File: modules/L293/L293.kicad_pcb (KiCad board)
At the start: 2 copper layers, 40.6 x 40.6 mm, 40 parts, among them J1 2, J10 11, J11 12, J12 13, J13 A0, J14 A1, J15 A2, J16 A3, J17 A4, J18 A5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

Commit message: Small fixes
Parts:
- moved C2 22.9 mm to (108.3, 62.8)
- moved J16 22.9 mm to (92.7, 52.1)
- moved J18 22.9 mm to (92.7, 57.1)
- moved J2 22.9 mm to (125.7, 57.1)
- moved J4 22.9 mm to (125.7, 52.1)
- moved JP1 22.9 mm to (95.9, 57.1)
- moved U2 22.9 mm to (119.0, 45.8)
- moved U3 22.9 mm to (119.0, 42.2)
- moved C1 22.9 mm to (116.1, 48.6)
- moved C5 22.9 mm to (97.8, 64.8)
- moved C6 22.9 mm to (104.8, 62.0)
- moved H1 22.9 mm to (92.7, 31.8)
- moved H2 22.9 mm to (92.7, 64.8)
- moved H3 22.9 mm to (125.7, 31.8)
- moved H4 22.9 mm to (125.7, 64.8)
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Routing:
- net (no net): track 5.72 -> 8.26 mm
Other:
- board text added: "28.03.2020"
- board text removed: "26.03.2020"

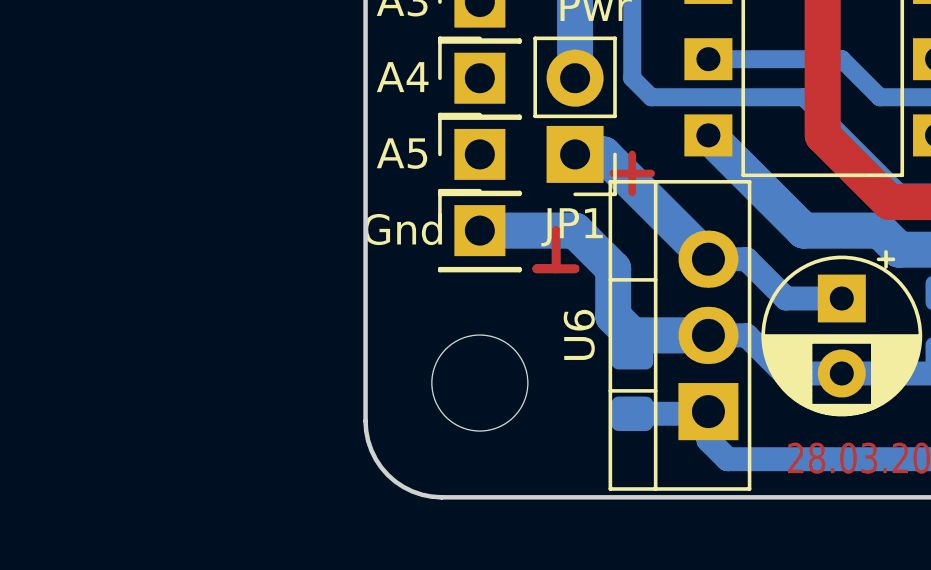
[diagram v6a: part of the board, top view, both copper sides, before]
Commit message: Motor shield v2 in work Attention! Pin numbers changed!
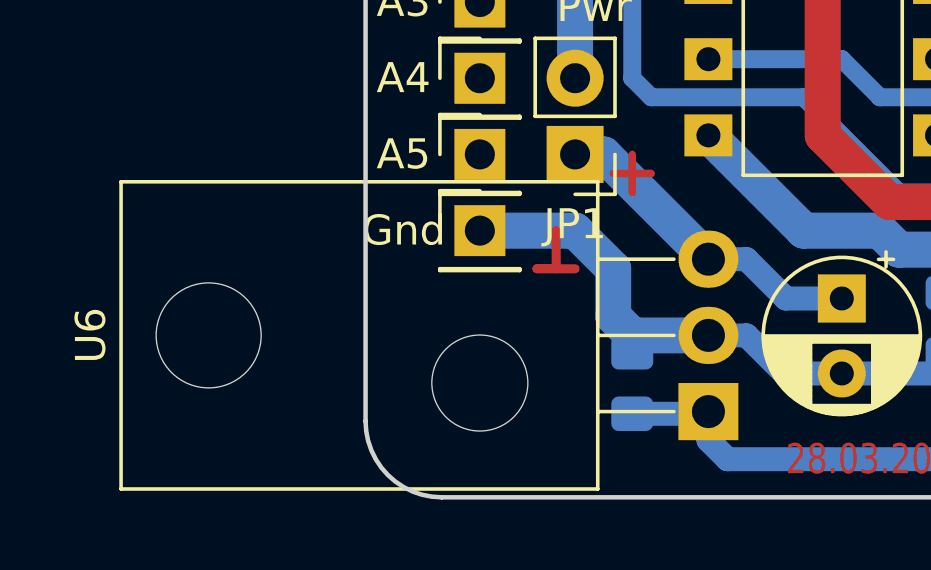
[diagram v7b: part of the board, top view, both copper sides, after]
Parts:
- U6: footprint Package_TO_SOT_THT:TO-220-3_Vertical -> Package_TO_SOT_THT:TO-220-3_Horizontal_TabDown
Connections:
- J10 pad 1: Net-(J10-Pad1) -> /M2-
- J4 pad 1: Net-(J4-Pad1) -> /PWM1
- J5 pad 1: Net-(J5-Pad1) -> /PWM2
- J7 pad 1: Net-(J7-Pad1) -> /M1+
- J8 pad 1: Net-(J8-Pad1) -> /M1-
- J9 pad 1: Net-(J9-Pad1) -> /M2+
- U1 pad 1: Net-(J3-Pad1) -> /M1+
- U2 pad 1: Net-(J4-Pad1) -> /M1-
- U3 pad 1: Net-(J5-Pad1) -> /M2+
- U4 pad 1: Net-(J6-Pad1) -> /M2-
- U5 pad 1: Net-(J9-Pad1) -> /PWM1
- U5 pad 9: Net-(J10-Pad1) -> /PWM2

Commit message: L293 in work.
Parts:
- moved JP1 21.0 mm to (96.2, 36.2), turned to 90 degrees
- moved C5 18.5 mm to (115.3, 58.7), turned to 0 degrees
- moved C4 17.6 mm to (100.6, 63.5), turned to 0 degrees
- moved C6 17.5 mm to (122.2, 60.6), turned to 180 degrees
- moved U6 16.2 mm to (113.7, 56.5), turned to 0 degrees
- moved C1 5.40 mm to (116.1, 43.2)
- moved C2 3.38 mm to (107.3, 66.0), turned to 270 degrees
- moved J21 3.18 mm to (115.6, 64.1)
- moved U4 2.78 mm to (119.0, 41.3)
- moved R1 2.29 mm to (122.2, 54.6), turned to 270 degrees
- moved U3 2.22 mm to (119.0, 44.5)
- moved U2 1.84 mm to (119.0, 47.6)
- moved U1 0.95 mm to (119.1, 50.8)
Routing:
- net /PWM1: track 0.00 -> 42.7 mm, vias 0 -> 1
- net Net-(J10-Pad1): track 37.6 -> 0.00 mm
- net VCC: track 66.6 -> 29.2 mm, vias 5 -> 4
- net Net-(J9-Pad1): track 27.2 -> 0.00 mm, vias 1 -> 0
- net GND: track 117.0 -> 97.9 mm
- net Net-(C2-Pad2): track 55.4 -> 37.0 mm
- net Net-(J6-Pad1): track 15.3 -> 0.00 mm
- net Net-(J5-Pad1): track 13.9 -> 0.00 mm
- net /M1+: track 0.00 -> 13.8 mm
- net /M2+: track 0.00 -> 13.5 mm
- net /M1-: track 0.00 -> 13.2 mm
- net Net-(J4-Pad1): track 12.2 -> 0.00 mm
- net /M2-: track 0.00 -> 12.1 mm
- net Net-(J3-Pad1): track 11.0 -> 0.00 mm
- net /PWM2: track 0.00 -> 7.22 mm
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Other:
- board text added: "07.04.2020"
- board text removed: "28.03.2020"
